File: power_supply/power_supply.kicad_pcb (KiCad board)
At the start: 2 copper layers, 100 x 100 mm, 36 parts, among them J1 Conn_01x02_Socket, J10 Conn_01x02_Socket, J11 Conn_01x02_Socket, J12 Conn_01x02_Socket, J13 Conn_01x02_Socket, J14 Conn_01x02_Socket, J15 Conn_01x02_Socket, J16 Conn_01x02_Socket, J17 Conn_01x02_Socket, J18 Conn_01x02_Socket, J19 Conn_01x02_Socket, J2 Conn_01x02_Socket, J20 Conn_01x02_Socket, J21 Conn_01x02_Pin, J22 Conn_01x02_Pin, J23 Conn_01x02_Socket, J24 Conn_01x02_Socket, J3 Conn_01x02_Socket, J4 Conn_01x02_Socket, J5 Conn_01x02_Socket, J6 Conn_01x02_Socket, J7 Conn_01x02_Socket, J8 Conn_01x02_Socket, J9 Conn_01x02_Socket

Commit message: 2024/11/05/23:24
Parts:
- moved C1 27.5 mm to (27.0, 60.3), turned to 90 degrees
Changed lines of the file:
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@@
 		)
 		(attr smd)
+		(fp_text user "${REFERENCE}"
+			(at 0 2.5 0)
+			(unlocked yes)
+			(layer "F.Fab")
+			(effects
+				(font
+					(size 1 1)
+					(thickness 0.15)
+				)
+			)
+		)
 		(pad "1" thru_hole circle
 			(at 0 0)
@@
 	(footprint "Connector_PinHeader_2.54mm:PinHeader_2x01_P2.54mm_Vertical"
 		(layer "F.Cu")
-		(at 15 35.5 -90)
+		(at 27 60.275 90)
 		(descr "Through hole straight pin header, 2x01, 2.54mm pitch, double rows")
 		(tags "Through hole pin header THT 2x01 2.54mm double row")
@@
 		)
 		(property "Footprint" "Connector_PinHeader_2.54mm:PinHeader_2x01_P2.54mm_Vertical"
-			(at 0 0 -90)
+			(at 0 0 90)
 			(unlocked yes)
 			(layer "F.Fab")
@@
 		)
 		(property "Datasheet" ""
-			(at 0 0 -90)
+			(at 0 0 90)
 			(unlocked yes)
 			(layer "F.Fab")
@@
 		)
 		(property "Description" "Unpolarized capacitor"
-			(at 0 0 -90)
+			(at 0 0 90)
 			(unlocked yes)
 			(layer "F.Fab")
@@
 		(attr through_hole)
 		(fp_line
-			(start -1.33 1.33)
+			(start 3.87 -1.33)
 			(end 3.87 1.33)
 			(stroke
@@
 		)
 		(fp_line
-			(start -1.33 1.27)
-			(end -1.33 1.33)
+			(start 1.27 -1.33)
+			(end 3.87 -1.33)
 			(stroke
 				(width 0.12)
@@
 		)
 		(fp_line
-			(start -1.33 1.27)
-			(end 1.27 1.27)
+			(start -1.33 -1.33)
+			(end 0 -1.33)
 			(stroke
 				(width 0.12)
@@
 		)
 		(fp_line
-			(start 1.27 1.27)
-			(end 1.27 -1.33)
+			(start -1.33 0)
+			(end -1.33 -1.33)
 			(stroke
 				(width 0.12)
@@
 		)
 		(fp_line
-			(start -1.33 0)
-			(end -1.33 -1.33)
+			(start 1.27 1.27)
+			(end 1.27 -1.33)
 			(stroke
 				(width 0.12)
@@
 		)
 		(fp_line
-			(start -1.33 -1.33)
-			(end 0 -1.33)
+			(start -1.33 1.27)
+			(end 1.27 1.27)
 			(stroke
 				(width 0.12)
@@
 		)
 		(fp_line
-			(start 1.27 -1.33)
-			(end 3.87 -1.33)
+			(start -1.33 1.27)
+			(end -1.33 1.33)
 			(stroke
 				(width 0.12)
@@
 		)
 		(fp_line
-			(start 3.87 -1.33)
+			(start -1.33 1.33)
 			(end 3.87 1.33)
 			(stroke
@@
 		)
 		(fp_line
-			(start -1.8 1.8)
-			(end 4.35 1.8)
+			(start 4.35 -1.8)
+			(end -1.8 -1.8)
 			(stroke
 				(width 0.05)
@@
 		)
 		(fp_line
-			(start 4.35 1.8)
-			(end 4.35 -1.8)
+			(start -1.8 -1.8)
+			(end -1.8 1.8)
 			(stroke
 				(width 0.05)
@@
 		)
 		(fp_line
-			(start -1.8 -1.8)
-			(end -1.8 1.8)
+			(start 4.35 1.8)
+			(end 4.35 -1.8)
 			(stroke
 				(width 0.05)
@@
 		)
 		(fp_line
-			(start 4.35 -1.8)
-			(end -1.8 -1.8)
+			(start -1.8 1.8)
+			(end 4.35 1.8)
 			(stroke
 				(width 0.05)
@@
 		)
 		(fp_line
-			(start -1.27 1.27)
-			(end -1.27 0)
+			(start 3.81 -1.27)
+			(end 3.81 1.27)
 			(stroke
 				(width 0.1)
@@
 		)
 		(fp_line
-			(start 3.81 1.27)
-			(end -1.27 1.27)
+			(start 0 -1.27)
+			(end 3.81 -1.27)
 			(stroke
 				(width 0.1)
@@
 		)
 		(fp_line
-			(start 0 -1.27)
-			(end 3.81 -1.27)
+			(start 3.81 1.27)
+			(end -1.27 1.27)
 			(stroke
 				(width 0.1)
@@
 		)
 		(fp_line
-			(start 3.81 -1.27)
-			(end 3.81 1.27)
+			(start -1.27 1.27)
+			(end -1.27 0)
 			(stroke
 				(width 0.1)
@@
 		)
 		(fp_text user "${REFERENCE}"
-			(at 1.27 0 0)
+			(at 1.27 0 360)
 			(layer "F.Fab")
 			(effects
@@
 		)
 		(pad "1" thru_hole rect
-			(at 0 0 270)
+			(at 0 0 90)
 			(size 1.7 1.7)
 			(drill 1)
@@
 		)
 		(pad "2" thru_hole oval
-			(at 2.54 0 270)
+			(at 2.54 0 90)
 			(size 1.7 1.7)
 			(drill 1)
@@
 	)
 	(gr_text "12VOUT\nMAX_3A"
-		(at 27 61.5 0)
+		(at 29.5 61.5 0)
 		(layer "F.SilkS")
 		(effects

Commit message: 2024/11/08
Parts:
- removed the G*** at (62.0, 20.0)
- removed the REF** at (107.0, 17.0)
- removed the REF** at (107.0, 107.0)
- added C2: C_Polarized, Capacitor_THT:CP_Radial_D10.0mm_P5.00mm, F.Cu at (20.4, 54.0)
- added C3: C_Polarized, Capacitor_THT:CP_Radial_D10.0mm_P5.00mm, F.Cu at (20.4, 65.0)
- added C4: C_Polarized, Capacitor_THT:CP_Radial_D10.0mm_P5.00mm, F.Cu at (20.4, 76.0)
- added C5: 0.33μF, Capacitor_SMD:C_0603_1608Metric_Pad1.08x0.95mm_HandSolder, F.Cu at (55.0, 57.0)
- added C6: 0.1μF, Capacitor_SMD:C_0603_1608Metric_Pad1.08x0.95mm_HandSolder, F.Cu at (56.5, 54.8)
- added C7: 0.33μF, Capacitor_SMD:C_0603_1608Metric_Pad1.08x0.95mm_HandSolder, F.Cu at (60.2, 54.9)
- added C8: 0.1μF, Capacitor_SMD:C_0603_1608Metric_Pad1.08x0.95mm_HandSolder, F.Cu at (64.7, 61.7)
- added D1: LED, LED_SMD:LED_0603_1608Metric_Pad1.05x0.95mm_HandSolder, F.Cu at (62.0, 87.2)
- added D2: LED, LED_SMD:LED_0603_1608Metric_Pad1.05x0.95mm_HandSolder, F.Cu at (65.0, 87.2)
- added D3: LED, LED_SMD:LED_0603_1608Metric_Pad1.05x0.95mm_HandSolder, F.Cu at (68.0, 87.2)
- added D4: OSHR1608C1A, LED_SMD:LED_0603_1608Metric_Pad1.05x0.95mm_HandSolder, F.Cu at (43.0, 89.0)
- added D5: GS1010FL, Diode_SMD:Nexperia_CFP3_SOD-123W, F.Cu at (47.5, 89.5)
- added D6: D, Diode_THT:D_5W_P12.70mm_Horizontal, F.Cu at (71.0, 76.0)
- added D7: D, Diode_THT:D_5W_P12.70mm_Horizontal, F.Cu at (75.5, 76.0)
- added D8: D, Diode_THT:D_5W_P12.70mm_Horizontal, F.Cu at (80.0, 76.0)
- added Q1: 2SC945L-K-T92-K, Package_TO_SOT_THT:TO-92_Inline, F.Cu at (50.2, 90.0)
- added R2: 300Ω, Resistor_SMD:R_0603_1608Metric_Pad0.98x0.95mm_HandSolder, F.Cu at (65.0, 83.7)
- added R3: 120Ω, Resistor_SMD:R_0603_1608Metric_Pad0.98x0.95mm_HandSolder, F.Cu at (68.0, 83.7)
- added R4: 1kΩ, Resistor_SMD:R_0603_1608Metric_Pad0.98x0.95mm_HandSolder, F.Cu at (45.0, 89.0)
- added R5: 1kΩ, Resistor_SMD:R_0603_1608Metric_Pad0.98x0.95mm_HandSolder, F.Cu at (55.9, 89.5)
- added R6: 10kΩ, Resistor_SMD:R_0603_1608Metric_Pad0.98x0.95mm_HandSolder, F.Cu at (55.9, 88.0)
- added SW1: SW_DIP_x04, 00a:KSD42, F.Cu at (78.5, 87.7)
- added U2: NJM2845DL1-33, 00a:TO-252-3_TabPin2, F.Cu at (67.4, 56.0)
- C1: value C -> C_Polarized; footprint Connector_PinHeader_2.54mm:PinHeader_2x01_P2.54mm_Vertical -> Capacitor_THT:CP_Radial_D10.0mm_P5.00mm
- G***: moved to B.Cu
- J1: value Conn_01x02_Socket -> XT60_IN
- J10, J11, J12, J13, J14, J15, J16, J9: value Conn_01x02_Socket -> XH_OUT
- J17, J18, J19, J20: value Conn_01x02_Socket -> XH_3.3V_OUT
- J2: value Conn_01x02_Socket -> Emergency Stop Switch
- J21, J22: value Conn_01x02_Pin -> XH_3.3V_OUT; footprint Connector_AMASS:AMASS_XT60-F_1x02_P7.20mm_Vertical -> Connector_JST:JST_XH_B2B-XH-A_1x02_P2.50mm_Vertical
- J23, J24: value Conn_01x02_Socket -> XH_3.3V_OUT; footprint Connector_AMASS:AMASS_XT60-F_1x02_P7.20mm_Vertical -> Connector_JST:JST_XH_B2B-XH-A_1x02_P2.50mm_Vertical
- J3, J4, J5: value Conn_01x02_Socket -> XT60_OUT
- J6, J7, J8: value Conn_01x02_Socket -> XT60_OUT; footprint Connector_JST:JST_XH_B2B-XH-A_1x02_P2.50mm_Vertical -> Connector_AMASS:AMASS_XT60-F_1x02_P7.20mm_Vertical
- R1: value 10 -> 1kΩ; footprint Resistor_THT:R_Axial_DIN0207_L6.3mm_D2.5mm_P10.16mm_Horizontal -> Resistor_SMD:R_0603_1608Metric_Pad0.98x0.95mm_HandSolder
- U1: value ~ -> NJM7805SDL1; footprint Connector_PinSocket_2.54mm:PinSocket_1x03_P2.54mm_Vertical -> 00a:TO-252-3_TabPin2
- U3: value ~ -> 953-1C-12DG-1; footprint footprints:3557-15_KEY -> 00a:953-1C-12DG-1
- U4: value ~ -> Y14H-1C-5DS; footprint 00a:1MS1-T1-B1-M1-Q-N-S -> 00a:Y14H-1C-5DS
- U5: value ~ -> Y14H-1C-5DS; footprint Connector_PinHeader_2.54mm:PinHeader_1x03_P2.54mm_Vertical -> 00a:Y14H-1C-5DS
- moved J13 75.5 mm to (53.5, 16.9), turned to 0 degrees
- moved J5 74.4 mm to (27.4, 38.8), turned to 0 degrees
- moved G*** 72.5 mm to (64.3, 85.7), turned to 180 degrees
- moved J21 69.6 mm to (73.0, 16.9), turned to 0 degrees
- moved J17 65.3 mm to (63.5, 16.9), turned to 0 degrees
- moved U5 63.0 mm to (61.7, 45.8), turned to 0 degrees
- moved J20 61.0 mm to (63.5, 40.3), turned to 0 degrees
- moved J18 61.0 mm to (63.5, 24.7), turned to 0 degrees
- moved J4 60.8 mm to (27.4, 28.5), turned to 0 degrees
- moved J12 60.7 mm to (44.0, 40.3), turned to 0 degrees
- moved J19 59.5 mm to (63.5, 32.5), turned to 0 degrees
- moved J1 57.8 mm to (29.3, 82.0), turned to 0 degrees
- moved J14 57.3 mm to (53.5, 24.7), turned to 0 degrees
- moved J11 55.8 mm to (44.0, 32.5), turned to 0 degrees
- moved J9 55.2 mm to (44.0, 16.9), turned to 0 degrees
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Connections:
- C1 pad 1: GND -> +12V_IN
- C1 pad 2: +12V_1 -> GND
- J1 pad 2: +12V_3 -> +12V_IN
- J10 pad 1: +12V_2 -> +5V_OUT
- J11 pad 1: +12V_2 -> +5V_OUT
- J12 pad 1: +12V_2 -> +5V_OUT
- J13 pad 1: +12V_2 -> +5V_OUT
- J14 pad 1: Net-(J14-Pin_1) -> +5V_OUT
- J15 pad 1: Net-(J14-Pin_1) -> +5V_OUT
- J16 pad 1: Net-(J14-Pin_1) -> +5V_OUT
- J17 pad 1: Net-(J14-Pin_1) -> +3.3V_OUT
- J18 pad 1: Net-(J14-Pin_1) -> +3.3V_OUT
- J19 pad 1: Net-(J14-Pin_1) -> +3.3V_OUT
- J2 pad 1: Net-(J14-Pin_1) -> Net-(D6-A)
- J2 pad 2: GND -> +5V_IN
- J20 pad 1: Net-(J14-Pin_1) -> +3.3V_OUT
- J21 pad 1: GND -> +3.3V_OUT
- J21 pad 2: +12V_1 -> GND
- J22 pad 1: +12V_2 -> +3.3V_OUT
- J22 pad 2: +12V_3 -> GND
- J23 pad 1: GND -> +3.3V_OUT
- J23 pad 2: +12V_3 -> GND
- J24 pad 1: GND -> +3.3V_OUT
- J24 pad 2: +12V_3 -> GND
- J3 pad 2: +12V_3 -> +12V_OUT
- J4 pad 2: +12V_3 -> +12V_OUT
- J5 pad 2: +12V_3 -> +12V_OUT
- J6 pad 1: +12V_2 -> GND
- J6 pad 2: GND -> +12V_OUT
- J7 pad 1: +12V_2 -> GND
- J7 pad 2: GND -> +12V_OUT
- J8 pad 1: +12V_2 -> GND
- J8 pad 2: GND -> +12V_OUT
- J9 pad 1: +12V_2 -> +5V_OUT
- R1 pad 1: Net-(R1-Pad1) -> Net-(D1-A)
- R1 pad 2: Net-(U5-OUT) -> +12V_OUT
- U1 pad 1: +12V_2 -> +12V_IN
- U1 pad 3: Net-(J14-Pin_1) -> +5V_IN
- U3 pad 1: +12V_1 -> +12V_IN
- U3 pad 2: +12V_1 -> Net-(D5-A)
- U3 pad 3: +12V_2 -> +12_IN
- U3 pad 4: +12V_2 -> unconnected-(U3-N.O.-Pad4)
- U4 pad 1: Net-(J14-Pin_1) -> +5V_OUT
- U4 pad 2: Net-(U5-OUT) -> unconnected-(U4-N.O.-Pad2)
- U4 pad 3: +12V_2 -> Net-(D7-K)
- U5 pad 1: GND -> +3.3V_OUT
- U5 pad 2: Net-(R1-Pad1) -> unconnected-(U5-N.O.-Pad2)
- U5 pad 3: Net-(U5-OUT) -> Net-(D8-K)
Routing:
- net Net-(J14-Pin_1): track 105.3 -> 0.00 mm
- net +5V_OUT: track 0.00 -> 91.4 mm, vias 0 -> 1
- net +5V_IN: track 0.00 -> 77.0 mm
- net Net-(U5-OUT): track 62.3 -> 0.00 mm
- net +3.3V_OUT: track 0.00 -> 61.4 mm, vias 0 -> 1
- net Net-(D7-K): track 0.00 -> 47.6 mm
- net Net-(D8-K): track 0.00 -> 43.3 mm
- net Net-(D6-K): track 0.00 -> 26.2 mm
- net +12V_OUT: track 0.00 -> 21.6 mm
- net Net-(D5-A): track 0.00 -> 16.9 mm
- net Net-(R1-Pad1): track 10.6 -> 0.00 mm
- net Net-(Q1-B): track 0.00 -> 3.94 mm
- net Net-(D4-K): track 0.00 -> 2.02 mm
- net Net-(D1-A): track 0.00 -> 1.80 mm
- net Net-(D3-A): track 0.00 -> 1.71 mm
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- added copper zone on F.Cu, net +12V_IN
- added copper zone on B.Cu, net +12V_OUT
- added copper zone on F.Cu, net +3.3V_IN
- added copper zone on F.Cu, net +3.3V_OUT
- added copper zone on F.Cu, net +5V_IN
- added copper zone on F.Cu, net +5V_OUT
- added copper zone on F.Cu, net GND
- added copper zone on F.Cu, net Net-(D6-A)
- removed copper zone on B.Cu, net +12V_1
- removed copper zone on F.Cu, net +12V_2
- removed copper zone on F.Cu, net +12V_3
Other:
- board size 100 x 100 mm -> 73 x 80 mm
- board text added: "https://github.com/syamei0/kicad/tree/master/power_supply"
- board text added: "power_supply_v3.0.0"
- board text added: "右下のスイッチで非常停止ボタンを 押した時に切る電源系統を 変更出来ます。 1:12V系統 2:5V系統 3:3.3V系統 4:無し"
- board text removed: "+"
- board text removed: "-"
- board text removed: "12V"
- board text removed: "12VIN"
- board text removed: "12VOUT MAX_35A"
- board text removed: "12VOUT MAX_3A"
- board text removed: "1MS1-T1-B1-M1-Q-N"
- board text removed: "3557-15"
- board text removed: "5V"
- board text removed: "5VOUT MAX_1.5A"
- board text removed: "DC voltmeter-Red"
- board text removed: "Power_v2.0.0"
- board text removed: "R_10Ω"
- board text removed: "switch"

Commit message: 2024/11/18
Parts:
- removed the REF** at (17.0, 17.0)
- removed the REF** at (17.0, 87.0)
- added G***: LOGO, 00a:MARC_rogo, B.Cu at (84.8, 73.5)
- added REF**: MountingHole_3.2mm_M3, MountingHole:MountingHole_3.2mm_M3, F.Cu at (104.0, 81.0)
- added REF**: MountingHole_3.2mm_M3, MountingHole:MountingHole_3.2mm_M3, F.Cu at (15.0, 81.0)
- added REF**: MountingHole_3.2mm_M3, MountingHole:MountingHole_3.2mm_M3, F.Cu at (104.0, 15.0)
- added REF**: MountingHole_3.2mm_M3, MountingHole:MountingHole_3.2mm_M3, F.Cu at (15.0, 15.0)
- D5: footprint Diode_SMD:Nexperia_CFP3_SOD-123W -> Diode_SMD:D_SOD-123F
- D6, D7, D8: footprint Diode_THT:D_5W_P12.70mm_Horizontal -> Diode_SMD:D_SOD-123F
- J1: footprint Connector_AMASS:AMASS_XT60-F_1x02_P7.20mm_Vertical -> Connector_AMASS:AMASS_XT60-M_1x02_P7.20mm_Vertical
- Q1: value 2SC945L-K-T92-K -> TTC014; footprint Package_TO_SOT_THT:TO-92_Inline -> 00a:TO-252-3_TabPin2
- R1, R4: value 1kΩ -> 10kΩ
- R2: value 300Ω -> 10kΩ
- R3: value 120Ω -> 10kΩ
- U4, U5: value Y14H-1C-5DS -> 134-1C-12DS; footprint 00a:Y14H-1C-5DS -> 00a:134-1C-12DS
- moved J1 65.0 mm to (23.2, 17.2), turned to -90 degrees
- moved Q1 59.4 mm to (73.0, 35.2), turned to 90 degrees
- moved J12 59.3 mm to (103.0, 35.0), turned to 90 degrees
- moved J3 58.2 mm to (85.6, 17.2), turned to -90 degrees
- moved J13 56.3 mm to (103.0, 43.8), turned to 90 degrees
- moved J11 53.0 mm to (95.8, 43.8), turned to 90 degrees
- moved J8 52.7 mm to (34.3, 17.2), turned to -90 degrees
- moved J17 52.1 mm to (81.0, 66.0), turned to 90 degrees
- moved R5 50.4 mm to (74.8, 42.8)
- moved J4 49.3 mm to (75.3, 17.2), turned to -90 degrees
- moved J10 48.4 mm to (88.5, 43.8), turned to 90 degrees
- moved J18 48.1 mm to (88.2, 66.0), turned to 90 degrees
- moved R6 47.7 mm to (71.1, 42.8), turned to 0 degrees
- moved J20 46.9 mm to (102.8, 66.0), turned to 90 degrees
- moved J19 46.3 mm to (95.5, 66.0), turned to 90 degrees
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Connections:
- J2 pad 2: +5V_IN -> +12V_IN
- Q1 pad 1: Net-(D5-A) -> Net-(Q1-B)
- Q1 pad 2: GND -> Net-(D5-A)
- Q1 pad 3: Net-(Q1-B) -> GND
- SW1 pad 1: +5V_IN -> +12V_IN
- SW1 pad 2: +5V_IN -> +12V_IN
- SW1 pad 3: +5V_IN -> +12V_IN
- SW1 pad 4: +5V_IN -> +12V_IN
- U3 pad 3: +12_IN -> +12V_IN
- U4 pad 1: +5V_OUT -> Net-(D7-K)
- U4 pad 2: unconnected-(U4-N.O.-Pad2) -> +5V_IN
- U4 pad 3: Net-(D7-K) -> +5V_OUT
- U4 pad 5: +5V_IN -> unconnected-(U4-Pad5)
- U5 pad 1: +3.3V_OUT -> Net-(D8-K)
- U5 pad 2: unconnected-(U5-N.O.-Pad2) -> +3.3V_IN
- U5 pad 3: Net-(D8-K) -> +3.3V_OUT
- U5 pad 5: +3.3V_IN -> unconnected-(U5-Pad5)
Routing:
- net +5V_IN: track 77.0 -> 0.00 mm
- net +12V_IN: track 0.00 -> 72.8 mm, vias 0 -> 2
- net +5V_OUT: track 91.4 -> 37.3 mm
- net Net-(D6-A): track 0.00 -> 48.9 mm
- net Net-(D6-K): track 26.2 -> 66.9 mm, vias 0 -> 1
- net Net-(D5-A): track 16.9 -> 57.5 mm
- net +12V_OUT: track 21.6 -> 50.0 mm, vias 0 -> 1
- net +3.3V_IN: track 0.00 -> 20.0 mm
- net +3.3V_OUT: track 61.4 -> 45.1 mm
- net Net-(D8-K): track 43.3 -> 52.6 mm, vias 0 -> 1
- net Net-(D7-K): track 47.6 -> 44.8 mm, vias 0 -> 1
- net Net-(Q1-B): track 3.94 -> 4.97 mm
- net Net-(D4-K): track 2.02 -> 2.62 mm
- net GND: vias 6 -> 0
- added copper zone on F.Cu, net +12V_OUT
- added copper zone on B.Cu, net +3.3V_OUT
- added copper zone on B.Cu, net +5V_OUT
- removed copper zone on B.Cu, net +12V_OUT
- removed copper zone on F.Cu, net +3.3V_IN
- removed copper zone on F.Cu, net +3.3V_OUT
- removed copper zone on F.Cu, net +5V_OUT
- removed copper zone on F.Cu, net Net-(D6-A)
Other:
- board size 73 x 80 mm -> 95 x 72 mm
- board text added: "12V"
- board text added: "3.3V"
- board text added: "5V"
- board text added: "D5,D6,D7,D8はダイオード D1,D2,D3,D4はLED"
- board text added: "INPUT"
- board text added: "https://partscabi.net/list/3c4d911b-a046-48f9-8f62-2c7ad6c0e181"
- board text added: "power_supply_v3.1.0"
- board text added: "左のスイッチで非常停止ボタンを 押した時に切る電源系統を 変更出来ます。 1:12V系統 2:5V系統 3:3.3V系統 4:無し"
- board text added: "非常停止スイッチ"
- board text removed: "power_supply_v3.0.0"
- board text removed: "右下のスイッチで非常停止ボタンを 押した時に切る電源系統を 変更出来ます。 1:12V系統 2:5V系統 3:3.3V系統 4:無し"

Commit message: 2024/11/19
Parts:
- removed C2, C3, C4: C_Polarized, Capacitor_THT:CP_Radial_D10.0mm_P5.00mm
- added F1: Fuse, 00a:3557-15_KEY, F.Cu at (70.8, 45.6)
- added F2: Fuse, 00a:3557-15_KEY, F.Cu at (61.5, 45.7)
- added F3: Fuse, 00a:3557-15_KEY, F.Cu at (52.3, 45.7)
- added F4: Fuse, 00a:3557-15_KEY, F.Cu at (43.0, 45.9)
- added F5: Fuse, 00a:3557-15_KEY, F.Cu at (37.4, 32.4)
- added F6: Fuse, 00a:3557-15_KEY, F.Cu at (29.8, 32.4)
- added F7: Fuse, 00a:3557-15_KEY, F.Cu at (84.0, 32.2)
- added J25: XT60_OUT, Connector_AMASS:AMASS_XT60-F_1x02_P7.20mm_Vertical, F.Cu at (82.2, 16.6)
- added JP1: SolderJumper_2_Open, Jumper:SolderJumper-2_P1.3mm_Open_Pad1.0x1.5mm, B.Cu at (74.5, 35.6)
- added JP2: SolderJumper_2_Open, Jumper:SolderJumper-2_P1.3mm_Open_Pad1.0x1.5mm, B.Cu at (65.0, 35.6)
- added JP3: SolderJumper_2_Open, Jumper:SolderJumper-2_P1.3mm_Open_Pad1.0x1.5mm, B.Cu at (55.8, 35.6)
- added JP4: SolderJumper_2_Open, Jumper:SolderJumper-2_P1.3mm_Open_Pad1.0x1.5mm, B.Cu at (46.5, 35.6)
- added JP5: SolderJumper_2_Open, Jumper:SolderJumper-2_P1.3mm_Open_Pad1.0x1.5mm, B.Cu at (37.8, 35.6)
- added JP6: SolderJumper_2_Open, Jumper:SolderJumper-2_P1.3mm_Open_Pad1.0x1.5mm, B.Cu at (29.8, 35.6)
- added JP7: SolderJumper_2_Open, Jumper:SolderJumper-2_P1.3mm_Open_Pad1.0x1.5mm, B.Cu at (83.8, 35.6)
- C5, C7: value 0.33μF -> 1μF
- moved J1 62.3 mm to (31.5, 79.0), turned to 180 degrees
- moved G*** 57.0 mm to (17.5, 57.5)
- moved G*** 57.0 mm to (30.0, 57.8)
- moved J17 48.7 mm to (100.8, 21.5), turned to 0 degrees
- moved J18 39.3 mm to (100.8, 28.7), turned to 0 degrees
- moved U3 36.3 mm to (14.7, 68.2), turned to 90 degrees
- moved U2 35.5 mm to (83.5, 65.1)
- moved C7 35.2 mm to (81.6, 72.4)
- moved C8 35.2 mm to (85.3, 72.4)
- moved J19 30.5 mm to (100.8, 36.0), turned to 0 degrees
- moved U5 28.1 mm to (77.0, 73.8), turned to 0 degrees
- moved J13 25.9 mm to (91.5, 67.0), turned to 0 degrees
- moved Q1 25.7 mm to (55.7, 54.2)
- moved R5 25.4 mm to (57.7, 61.5)
- moved R6 25.4 mm to (53.9, 61.5)
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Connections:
- C1 pad 1: +12V_IN -> +12V_OUT
- J3 pad 2: +12V_OUT -> XT_OUT_1
- J4 pad 2: +12V_OUT -> XT_OUT_2
- J5 pad 2: +12V_OUT -> XT_OUT_3
- J6 pad 2: +12V_OUT -> XT_OUT_4
- J7 pad 2: +12V_OUT -> XT_OUT_5
- J8 pad 2: +12V_OUT -> XT_OUT_6
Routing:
- net +5V_IN: track 0.00 -> 39.4 mm
- net Net-(D6-K): track 66.9 -> 27.7 mm
- net +12V_IN: track 72.8 -> 102.8 mm, vias 2 -> 0
- net Net-(D5-A): track 57.5 -> 34.2 mm
- net Net-(D8-K): track 52.6 -> 35.7 mm, vias 1 -> 0
- net +3.3V_IN: track 20.0 -> 5.77 mm
- net Net-(D6-A): track 48.9 -> 36.6 mm, vias 0 -> 2
- net +5V_OUT: track 37.3 -> 48.2 mm, vias 1 -> 0
- net +12V_OUT: track 50.0 -> 44.4 mm, vias 1 -> 0
- net Net-(D7-K): track 44.8 -> 39.5 mm, vias 1 -> 0
- net +3.3V_OUT: track 45.1 -> 42.3 mm, vias 1 -> 0
- net Net-(D4-K): track 2.62 -> 3.47 mm
- net GND: vias 0 -> 31
- added copper zone on B.Cu, net +12V_IN
- added copper zone on B.Cu, net +12V_OUT
- added copper zone on B.Cu, net XT_OUT_1
- added copper zone on B.Cu, net XT_OUT_2
- added copper zone on B.Cu, net XT_OUT_3
- added copper zone on B.Cu, net XT_OUT_4
- added copper zone on B.Cu, net XT_OUT_5
- added copper zone on B.Cu, net XT_OUT_6
- added copper zone on B.Cu, net XT_OUT_7
- removed copper zone on F.Cu, net +12V_IN
- removed copper zone on F.Cu, net +12V_OUT
- removed copper zone on F.Cu, net +5V_IN
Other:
- board text added: "2024/11/19 Yamamoto Maku"
- board text added: "D5,D6,D7,D8はダイオード D1,D2,D3,D4はLED JPをつなぐとフューズ無しで動作します"
- board text added: "左下のスイッチで非常停止ボタンを 押した時に切る電源系統を 変更出来ます。 1:12V系統 2:5V系統 3:3.3V系統 4:無し"
- board text removed: "D5,D6,D7,D8はダイオード D1,D2,D3,D4はLED"
- board text removed: "左のスイッチで非常停止ボタンを 押した時に切る電源系統を 変更出来ます。 1:12V系統 2:5V系統 3:3.3V系統 4:無し"

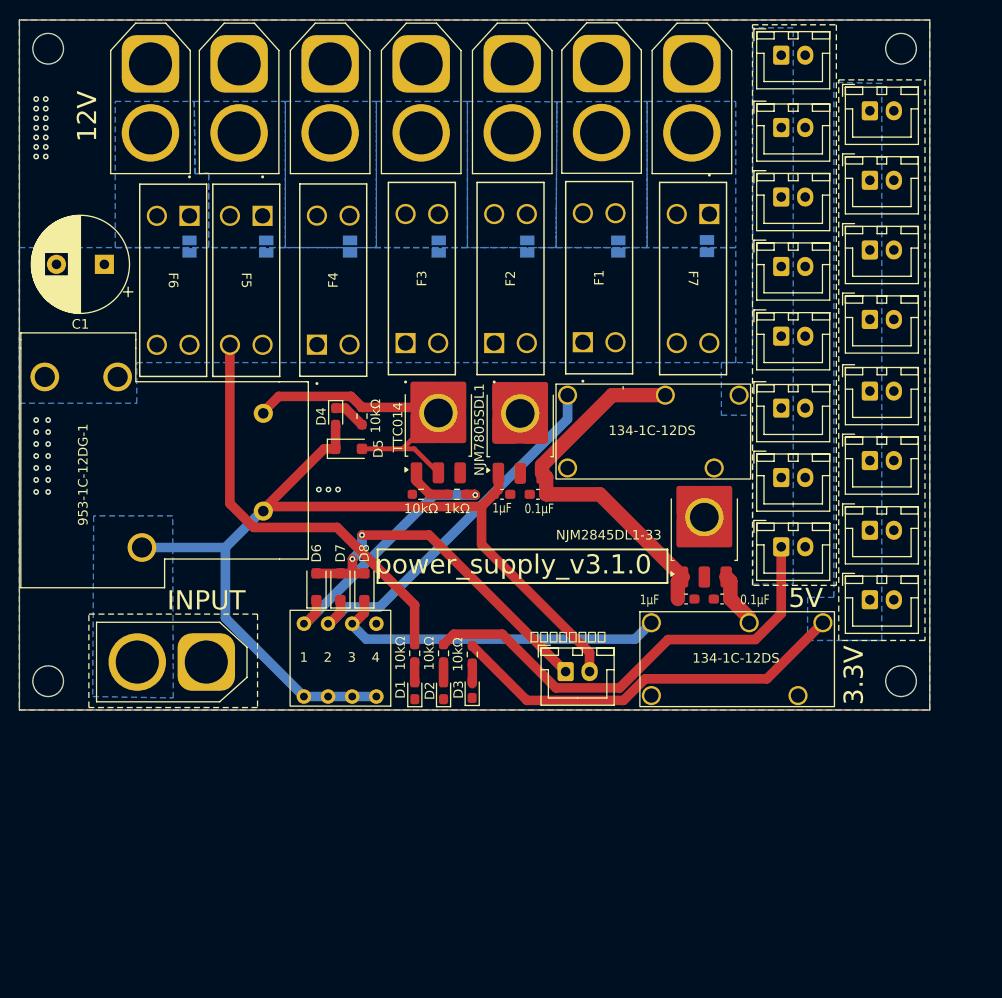
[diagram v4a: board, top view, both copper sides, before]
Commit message: 逆起電力用ダイオード追加,小型リレーのフットプリント修正,大型リレーのスイッチを反転
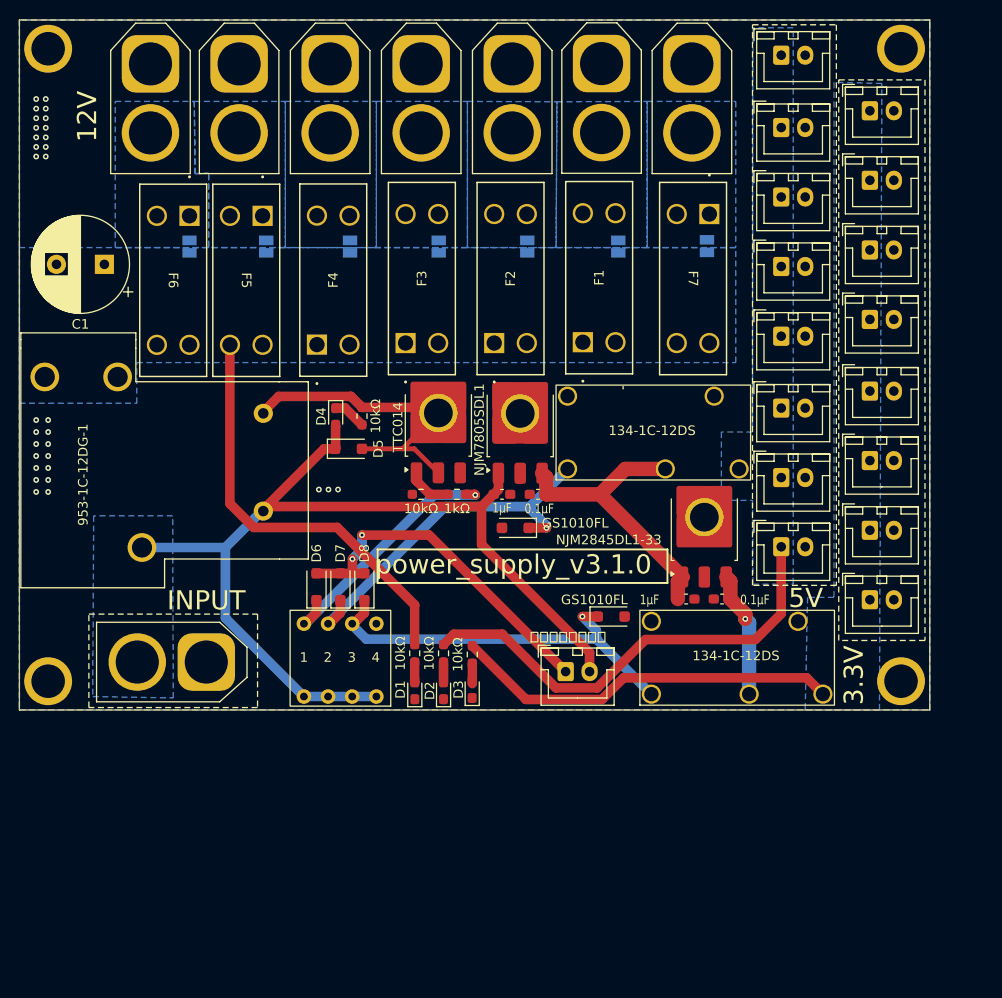
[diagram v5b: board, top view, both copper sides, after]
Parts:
- removed the REF** at (104.0, 81.0)
- removed the REF** at (15.0, 81.0)
- removed the REF** at (104.0, 15.0)
- removed the REF** at (15.0, 15.0)
- added D10: GS1010FL, Diode_SMD:D_SOD-123F, F.Cu at (73.8, 74.2)
- added D9: GS1010FL, Diode_SMD:D_SOD-123F, F.Cu at (63.8, 65.0)
- added REF**: hole_M3, 00a:hole_M3, F.Cu at (104.0, 81.0)
- added REF**: hole_M3, 00a:hole_M3, F.Cu at (104.0, 15.0)
- added REF**: hole_M3, 00a:hole_M3, F.Cu at (15.0, 81.0)
- added REF**: hole_M3, 00a:hole_M3, F.Cu at (15.0, 15.0)
- moved U5 0.25 mm to (77.0, 73.5)
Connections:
- U3 pad 4: unconnected-(U3-N.O.-Pad4) -> +12V_OUT
- U3 pad 5: +12V_OUT -> unconnected-(U3-N.C.-Pad5)
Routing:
- net +5V_IN: track 39.4 -> 30.6 mm
- net +3.3V_IN: track 5.77 -> 13.2 mm, vias 0 -> 1
- net Net-(D10-K): track 35.7 -> 42.5 mm, vias 0 -> 1
- net +3.3V_OUT: track 42.3 -> 40.5 mm
- net Net-(D7-K): track 39.5 -> 39.6 mm, vias 0 -> 1
